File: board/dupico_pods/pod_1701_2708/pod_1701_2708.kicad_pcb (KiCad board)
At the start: 2 copper layers, 15 parts, among them J1 dupico connector, J2 1702A, J3 2708, J4 Conn_01x06, U1 RD-0512D, U2 LM7905_TO220, U3 LM7909_TO220

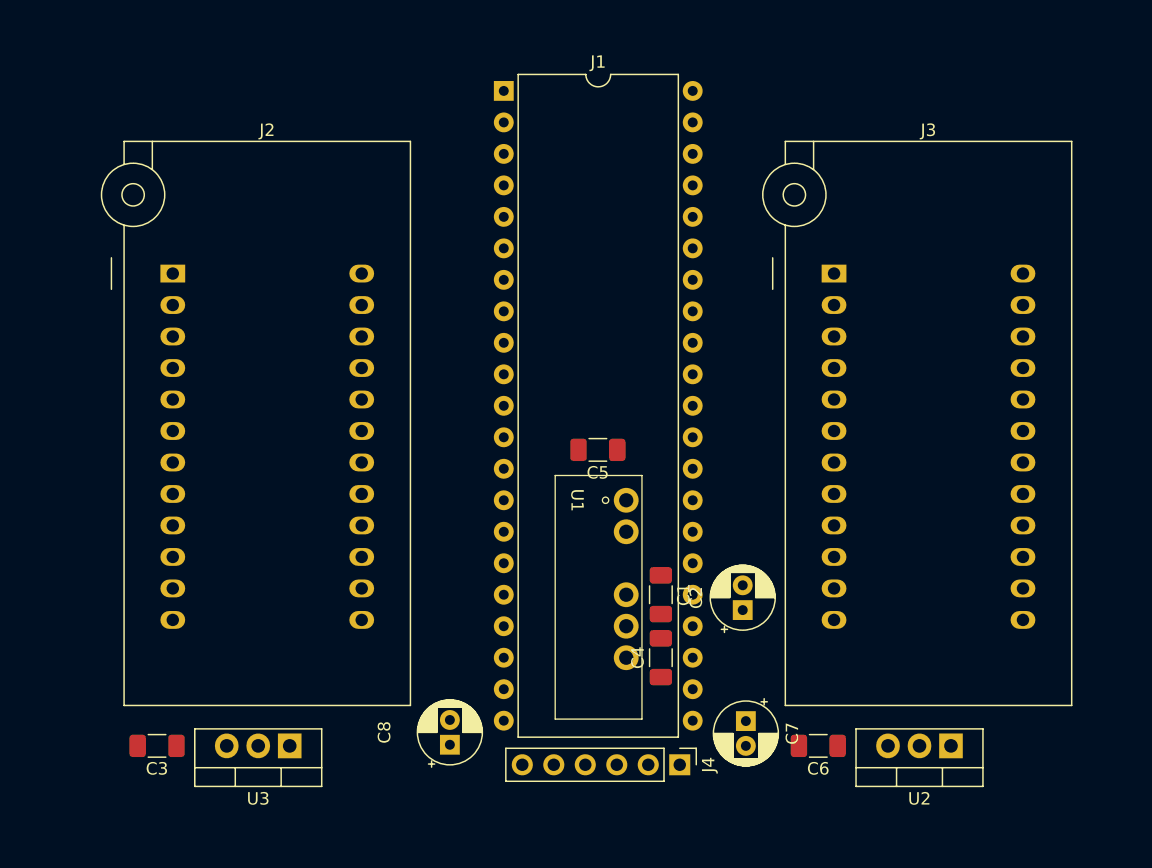
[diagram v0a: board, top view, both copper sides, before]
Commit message: Add automatic routing for pod
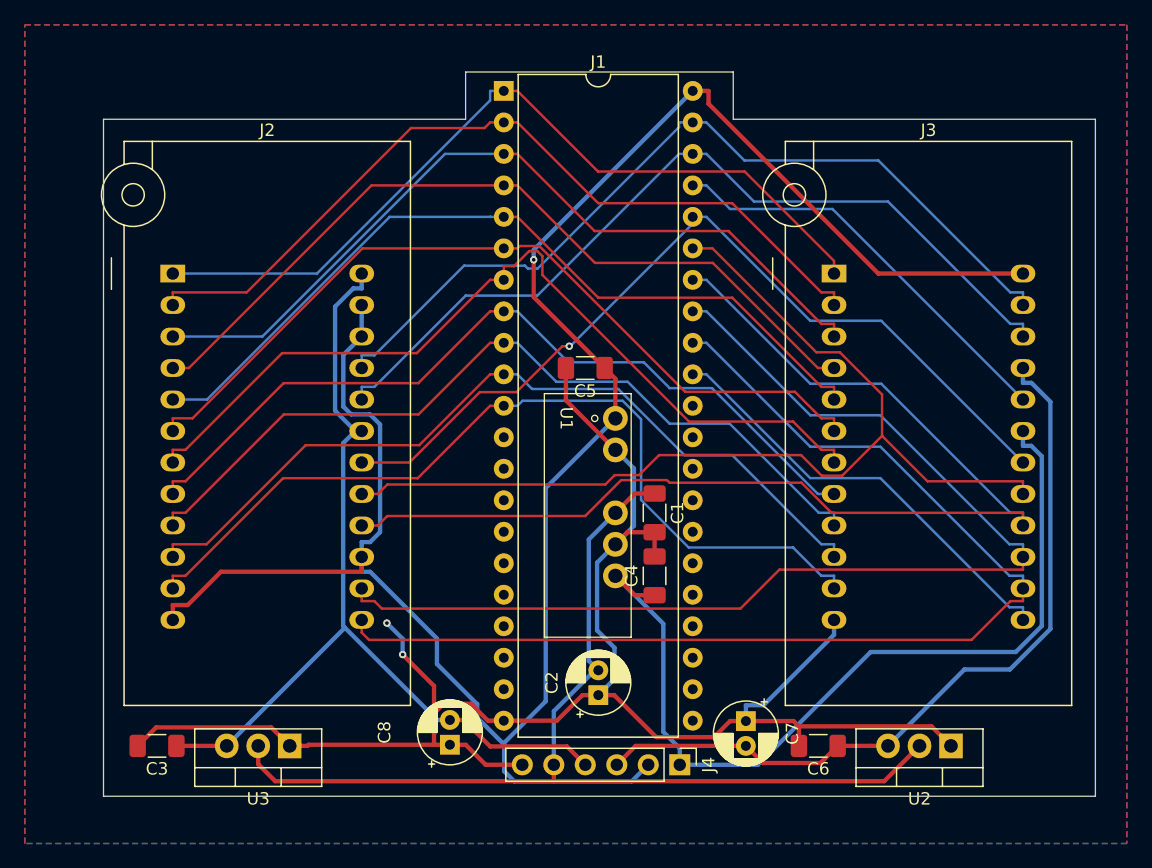
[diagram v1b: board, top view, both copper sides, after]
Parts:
- moved C2 13.5 mm to (90.7, 88.4)
- moved C5 6.68 mm to (89.7, 62.0)
- moved U1 6.66 mm to (87.6, 66.0)
- moved C1 6.62 mm to (95.2, 73.7)
- moved C4 6.62 mm to (95.2, 78.7)
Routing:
- net VCC: track 0.00 -> 175.6 mm, vias 0 -> 1
- net GND: track 0.00 -> 142.2 mm, vias 0 -> 2
- net /ZIF_36: track 0.00 -> 92.4 mm
- net /ZIF_35: track 0.00 -> 92.4 mm
- net /ZIF_34: track 0.00 -> 92.4 mm
- net -12V: track 0.00 -> 84.8 mm
- net /ZIF_37: track 0.00 -> 82.7 mm
- net -9V: track 0.00 -> 73.0 mm
- net +12V: track 0.00 -> 71.8 mm
- net /ZIF_11: track 0.00 -> 70.9 mm
- net /ZIF_38: track 0.00 -> 70.3 mm, vias 0 -> 1
- net /ZIF_7: track 0.00 -> 70.2 mm
- net /ZIF_41: track 0.00 -> 69.3 mm
- net /ZIF_40: track 0.00 -> 68.8 mm
- net /ZIF_6: track 0.00 -> 66.9 mm
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- added copper zone on B.Cu, net GND
- added copper zone on F.Cu, net GND
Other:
- board outline added: 80 x 58.4 mm
